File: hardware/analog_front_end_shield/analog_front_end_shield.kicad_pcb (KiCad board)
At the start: 4 copper layers, 68.6 x 53.3 mm, 43 parts, among them J1 640456-3, J2 S3B-EH(LF)(SN), J3 Conn_01x08, J4 Conn_01x06, J6 Conn_01x10, J7 Conn_01x08, J8 PPTC062LFBN-RC, U1 LMT84LPM, U2 TLV2472AIP

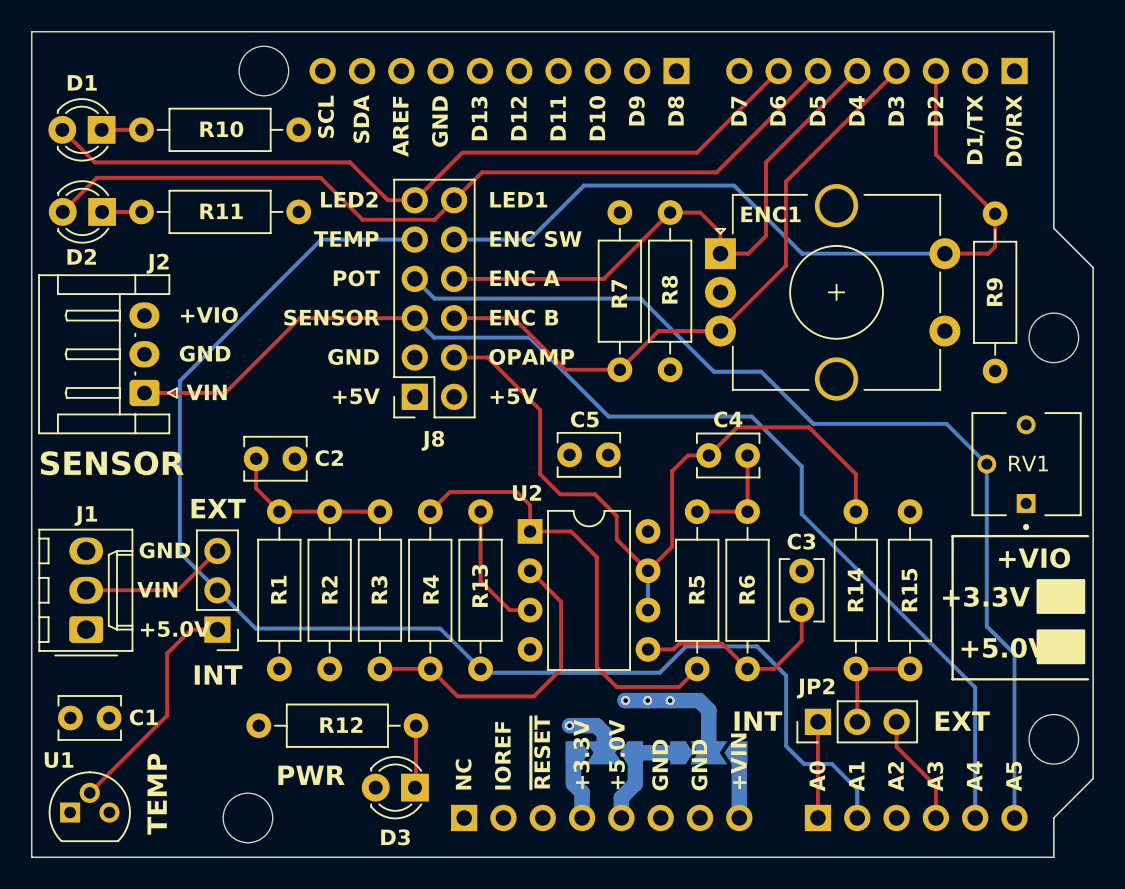
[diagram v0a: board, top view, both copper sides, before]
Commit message: AFE board version correction
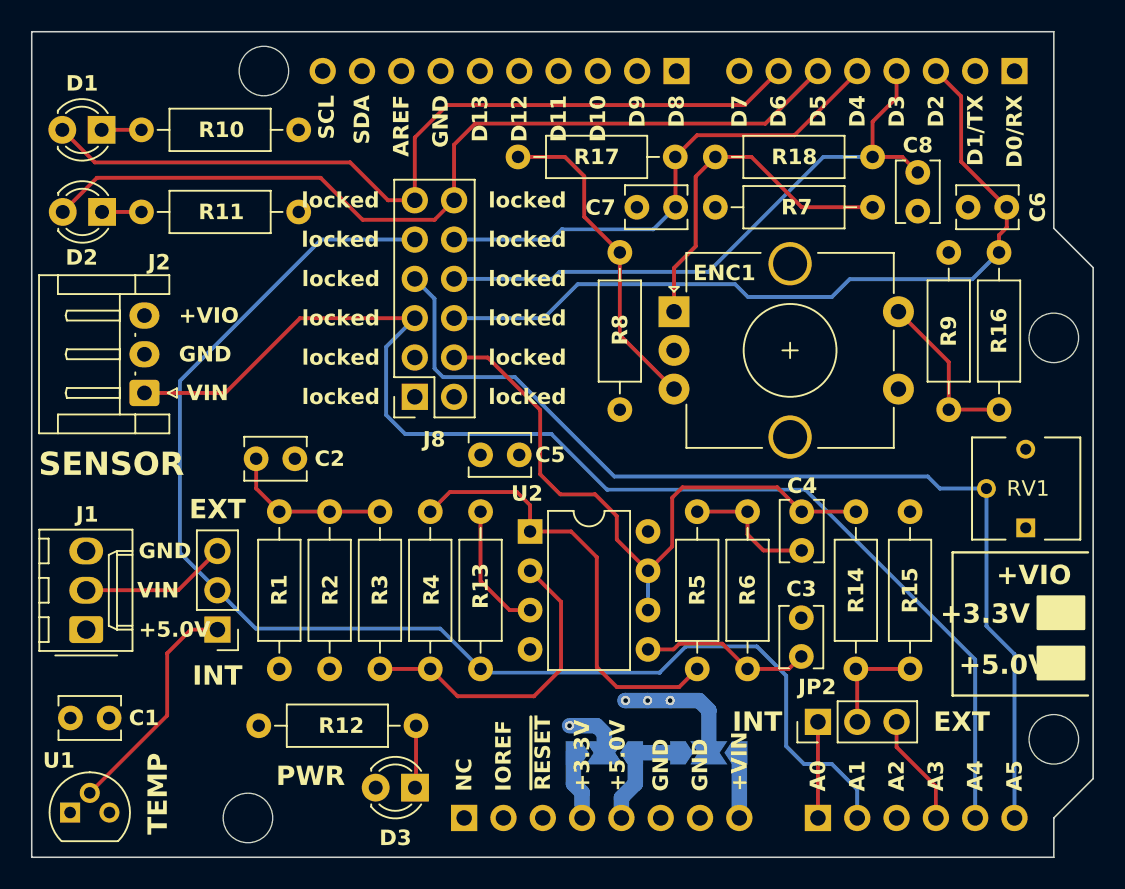
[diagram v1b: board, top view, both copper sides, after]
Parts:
- added C6: 10000pF, analog_front_end:C_Disc_D3.8mm_W2.6mm_P2.50mm, F.Cu at (115.0, 87.0)
- added C7: 10000pF, analog_front_end:C_Disc_D3.8mm_W2.6mm_P2.50mm, F.Cu at (93.6, 87.0)
- added C8: 10000pF, analog_front_end:C_Disc_D3.8mm_W2.6mm_P2.50mm, F.Cu at (109.2, 84.8)
- added R16: 4.7K, analog_front_end:R_Axial_DIN0207_L6.3mm_D2.5mm_P10.16mm_Horizontal, F.Cu at (114.5, 89.9)
- added R17: 4.7K, analog_front_end:R_Axial_DIN0207_L6.3mm_D2.5mm_P10.16mm_Horizontal, F.Cu at (93.6, 83.8)
- added R18: 4.7K, analog_front_end:R_Axial_DIN0207_L6.3mm_D2.5mm_P10.16mm_Horizontal, F.Cu at (106.3, 83.8)
- C1, C2, C3, C4, C5: footprint Capacitor_THT:C_Disc_D3.8mm_W2.6mm_P2.50mm -> analog_front_end:C_Disc_D3.8mm_W2.6mm_P2.50mm
- D1, D2, D3: footprint LED_THT:LED_D3.0mm -> analog_front_end:LED_D3.0mm
- ENC1: footprint Rotary_Encoder:RotaryEncoder_Alps_EC12E-Switch_Vertical_H20mm_CircularMountingHoles -> analog_front_end:RotaryEncoder_Alps_EC12E-Switch_Vertical_H20mm_CircularMountingHoles
- H1, H2, H3, H4: footprint MountingHole:MountingHole_3.2mm_M3 -> analog_front_end:MountingHole_3.2mm_M3
- J1: footprint Connector_Molex:Molex_KK-254_AE-6410-03A_1x03_P2.54mm_Vertical -> analog_front_end:Molex_KK-254_AE-6410-03A_1x03_P2.54mm_Vertical
- J2: footprint Connector_JST:JST_EH_S3B-EH_1x03_P2.50mm_Horizontal -> analog_front_end:JST_EH_S3B-EH_1x03_P2.50mm_Horizontal
- J3, J7: footprint Connector_PinHeader_2.54mm:PinHeader_1x08_P2.54mm_Vertical -> analog_front_end:PinHeader_1x08_P2.54mm_Vertical
- J4: footprint Connector_PinHeader_2.54mm:PinHeader_1x06_P2.54mm_Vertical -> analog_front_end:PinHeader_1x06_P2.54mm_Vertical
- J6: footprint Connector_PinHeader_2.54mm:PinHeader_1x10_P2.54mm_Vertical -> analog_front_end:PinHeader_1x10_P2.54mm_Vertical
- J8: footprint Connector_PinSocket_2.54mm:PinSocket_2x06_P2.54mm_Vertical -> analog_front_end:PinSocket_2x06_P2.54mm_Vertical
- JP1, JP2: footprint Connector_PinHeader_2.54mm:PinHeader_1x03_P2.54mm_Vertical -> analog_front_end:PinHeader_1x03_P2.54mm_Vertical
- JP3, JP4: footprint Jumper:SolderJumper-3_P2.0mm_Open_TrianglePad1.0x1.5mm -> analog_front_end:SolderJumper-3_P2.0mm_Open_TrianglePad1.0x1.5mm
- R1, R10, R11, R12, R13, R14, R15, R2, R3, R4, R5, R6, R7, R8, R9: footprint Resistor_THT:R_Axial_DIN0207_L6.3mm_D2.5mm_P10.16mm_Horizontal -> analog_front_end:R_Axial_DIN0207_L6.3mm_D2.5mm_P10.16mm_Horizontal
- REF**: footprint Symbol:OSHW-Logo2_9.8x8mm_SilkScreen -> analog_front_end:OSHW-Logo2_9.8x8mm_SilkScreen
- RV1: footprint Temp:TRIM_3362P-1-103LF -> analog_front_end:TRIM_3362P-1-103LF
- U1: footprint Package_TO_SOT_THT:TO-92 -> analog_front_end:TO-92
- U2: footprint Package_DIP:DIP-8_W7.62mm -> analog_front_end:DIP-8_W7.62mm
- moved R9 8.23 mm to (111.2, 89.9), turned to -90 degrees
- moved C4 7.06 mm to (101.8, 109.2), turned to 90 degrees
- moved R7 6.18 mm to (96.2, 87.0), turned to 0 degrees
- moved C5 5.75 mm to (83.5, 103.0)
- moved ENC1 4.80 mm to (93.5, 93.8)
- moved R8 4.15 mm to (90.0, 100.1)
- moved C3 3.03 mm to (101.7, 116.0)
- moved RV1 1.58 mm to (116.2, 105.2)
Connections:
- ENC1 pad A: /ENC_A -> Net-(ENC1-PadA)
- ENC1 pad B: /ENC_B -> Net-(ENC1-PadB)
- ENC1 pad S1: /ENC_SW -> Net-(ENC1-PadS1)
- J7 pad 4: /ENC_B -> /ENC_A
- J7 pad 5: /ENC_A -> /ENC_B
- J8 pad 10: /ENC_SW -> /ENC_B
- J8 pad 6: /ENC_B -> /ENC_SW
- R7 pad 2: /ENC_B -> Net-(ENC1-PadA)
- R8 pad 2: /ENC_A -> Net-(ENC1-PadB)
- R9 pad 2: /ENC_SW -> Net-(ENC1-PadS1)
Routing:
- net Net-(ENC1-PadA): track 0.00 -> 22.6 mm
- net Net-(ENC1-PadB): track 0.00 -> 21.0 mm
- net Net-(ENC1-PadS1): track 0.00 -> 10.9 mm
- net /ENC_B: track 41.1 -> 32.5 mm
- net /OPA_OUT: track 47.9 -> 42.3 mm
- net /IR_VOUT: track 75.8 -> 81.3 mm
- net Net-(U2B-+): track 13.5 -> 11.1 mm
- net /ENC_A: track 37.4 -> 39.8 mm
- net /LED1: track 51.6 -> 54.0 mm
- net /LED2: track 54.8 -> 56.9 mm
- net Net-(C4-Pad1): track 6.88 -> 8.65 mm
- net /POT: track 65.5 -> 67.2 mm
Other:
- board text added: "MAY 2023"
- board text added: "REV C"
- board text added: "locked"
- board text removed: "APR 2023"
- board text removed: "ENC A"
- board text removed: "ENC B"
- board text removed: "ENC SW"
- board text removed: "LED1"
- board text removed: "LED2"
- board text removed: "OPAMP"
- board text removed: "POT"
- board text removed: "REV B"
- board text removed: "https://github.com/UofTPhyEssSW/Student-Workshop-Course-L1"
